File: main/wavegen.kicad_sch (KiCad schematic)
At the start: 98 parts, among them U18 CD4046, U19 CD4046, U20 CD4017, U21 CD4017, U22 TL072CP, U23 TL072CP, U24 CD4046, U25 CD4046, U26 CD4017, U27 CD4017

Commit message: Switch to Thonk jacks.
Reduces use of extended parts.
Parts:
- C52, C53, C70, C71: footprint Capacitor_SMD:C_0805_2012Metric_Pad1.18x1.45mm_HandSolder -> Capacitor_SMD:C_0603_1608Metric_Pad1.08x0.95mm_HandSolder; LCSC Part # C282698 -> C519401
- C64, C65, C74, C75: footprint Capacitor_SMD:C_0805_2012Metric_Pad1.18x1.45mm_HandSolder -> Capacitor_SMD:C_0603_1608Metric_Pad1.08x0.95mm_HandSolder; LCSC Part # C107114 -> C1658
- U20, U21, U26, U27: LCSC Part # C11349 -> C356694
- U22, U23: LCSC Part # C67473 -> C6961
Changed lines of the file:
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@@
       (effects (font (size 1.27 1.27)) hide)
     )
-    (property "LCSC Part #" "C11349" (id 5) (at 215.265 113.03 0)
+    (property "LCSC Part #" "C356694" (id 5) (at 215.265 113.03 0)
       (effects (font (size 1.27 1.27)) hide)
     )
@@
       (effects (font (size 1.27 1.27)) hide)
     )
-    (property "LCSC Part #" "C67473" (id 6) (at 125.73 37.465 0)
+    (property "LCSC Part #" "C6961" (id 6) (at 125.73 37.465 0)
       (effects (font (size 1.27 1.27)) hide)
     )
@@
       (effects (font (size 1.27 1.27)) (justify left))
     )
-    (property "Footprint" "Capacitor_SMD:C_0805_2012Metric_Pad1.18x1.45mm_HandSolder" (id 2) (at 264.16 19.05 0)
+    (property "Footprint" "Capacitor_SMD:C_0603_1608Metric_Pad1.08x0.95mm_HandSolder" (id 2) (at 264.16 19.05 0)
       (effects (font (size 1.27 1.27)) hide)
     )
@@
       (effects (font (size 1.27 1.27)) hide)
     )
-    (property "LCSC Part #" "C107114" (id 5) (at 264.16 19.05 0)
+    (property "LCSC Part #" "C1658" (id 5) (at 264.16 19.05 0)
       (effects (font (size 1.27 1.27)) hide)
     )
@@
       (effects (font (size 1.27 1.27)) hide)
     )
-    (property "LCSC Part #" "C67473" (id 6) (at 126.365 107.95 0)
+    (property "LCSC Part #" "C6961" (id 6) (at 126.365 107.95 0)
       (effects (font (size 1.27 1.27)) hide)
     )
@@
       (effects (font (size 1.27 1.27)) (justify left))
     )
-    (property "Footprint" "Capacitor_SMD:C_0805_2012Metric_Pad1.18x1.45mm_HandSolder" (id 2) (at 126.365 19.05 0)
+    (property "Footprint" "Capacitor_SMD:C_0603_1608Metric_Pad1.08x0.95mm_HandSolder" (id 2) (at 126.365 19.05 0)
       (effects (font (size 1.27 1.27)) hide)
     )
@@
       (effects (font (size 1.27 1.27)) hide)
     )
-    (property "LCSC Part #" "C107114" (id 5) (at 126.365 19.05 0)
+    (property "LCSC Part #" "C1658" (id 5) (at 126.365 19.05 0)
       (effects (font (size 1.27 1.27)) hide)
     )
@@
       (effects (font (size 1.27 1.27)) (justify left))
     )
-    (property "Footprint" "Capacitor_SMD:C_0805_2012Metric_Pad1.18x1.45mm_HandSolder" (id 2) (at 264.16 89.535 0)
+    (property "Footprint" "Capacitor_SMD:C_0603_1608Metric_Pad1.08x0.95mm_HandSolder" (id 2) (at 264.16 89.535 0)
       (effects (font (size 1.27 1.27)) hide)
     )
@@
       (effects (font (size 1.27 1.27)) hide)
     )
-    (property "LCSC Part #" "C107114" (id 5) (at 264.16 89.535 0)
+    (property "LCSC Part #" "C1658" (id 5) (at 264.16 89.535 0)
       (effects (font (size 1.27 1.27)) hide)
     )
@@
       (effects (font (size 1.27 1.27)) hide)
     )
-    (property "LCSC Part #" "C67473" (id 6) (at 262.255 37.465 0)
+    (property "LCSC Part #" "C6961" (id 6) (at 262.255 37.465 0)
       (effects (font (size 1.27 1.27)) hide)
     )
@@
       (effects (font (size 1.27 1.27)) hide)
     )
-    (property "LCSC Part #" "C11349" (id 5) (at 77.47 42.545 0)
+    (property "LCSC Part #" "C356694" (id 5) (at 77.47 42.545 0)
       (effects (font (size 1.27 1.27)) hide)
     )
@@
       (effects (font (size 1.27 1.27)) (justify left))
     )
-    (property "Footprint" "Capacitor_SMD:C_0805_2012Metric_Pad1.18x1.45mm_HandSolder" (id 2) (at 127 89.535 0)
+    (property "Footprint" "Capacitor_SMD:C_0603_1608Metric_Pad1.08x0.95mm_HandSolder" (id 2) (at 127 89.535 0)
       (effects (font (size 1.27 1.27)) hide)
     )
@@
       (effects (font (size 1.27 1.27)) hide)
     )
-    (property "LCSC Part #" "C107114" (id 5) (at 127 89.535 0)
+    (property "LCSC Part #" "C1658" (id 5) (at 127 89.535 0)
       (effects (font (size 1.27 1.27)) hide)
     )
@@
       (effects (font (size 1.27 1.27)) hide)
     )
-    (property "LCSC Part #" "C11349" (id 5) (at 77.47 113.03 0)
+    (property "LCSC Part #" "C356694" (id 5) (at 77.47 113.03 0)
       (effects (font (size 1.27 1.27)) hide)
     )
@@
       (effects (font (size 1.27 1.27)) (justify left))
     )
-    (property "Footprint" "Capacitor_SMD:C_0805_2012Metric_Pad1.18x1.45mm_HandSolder" (id 2) (at 18.415 109.22 0)
+    (property "Footprint" "Capacitor_SMD:C_0603_1608Metric_Pad1.08x0.95mm_HandSolder" (id 2) (at 18.415 109.22 0)
       (effects (font (size 1.27 1.27)) hide)
     )
@@
       (effects (font (size 1.27 1.27)) hide)
     )
-    (property "LCSC Part #" "C282698" (id 5) (at 18.415 109.22 0)
+    (property "LCSC Part #" "C519401" (id 5) (at 18.415 109.22 0)
       (effects (font (size 1.27 1.27)) hide)
     )
@@
       (effects (font (size 1.27 1.27)) (justify left))
     )
-    (property "Footprint" "Capacitor_SMD:C_0805_2012Metric_Pad1.18x1.45mm_HandSolder" (id 2) (at 156.21 38.735 0)
+    (property "Footprint" "Capacitor_SMD:C_0603_1608Metric_Pad1.08x0.95mm_HandSolder" (id 2) (at 156.21 38.735 0)
       (effects (font (size 1.27 1.27)) hide)
     )
@@
       (effects (font (size 1.27 1.27)) hide)
     )
-    (property "LCSC Part #" "C282698" (id 5) (at 156.21 38.735 0)
+    (property "LCSC Part #" "C519401" (id 5) (at 156.21 38.735 0)
       (effects (font (size 1.27 1.27)) hide)
     )
@@
       (effects (font (size 1.27 1.27)) hide)
     )
-    (property "LCSC Part #" "C67473" (id 6) (at 262.255 107.95 0)
+    (property "LCSC Part #" "C6961" (id 6) (at 262.255 107.95 0)
       (effects (font (size 1.27 1.27)) hide)
     )
@@
       (effects (font (size 1.27 1.27)) hide)
     )
-    (property "LCSC Part #" "C11349" (id 5) (at 215.265 42.545 0)
+    (property "LCSC Part #" "C356694" (id 5) (at 215.265 42.545 0)
       (effects (font (size 1.27 1.27)) hide)
     )
@@
       (effects (font (size 1.27 1.27)) hide)
     )
-    (property "LCSC Part #" "C67473" (id 4) (at 124.46 160.655 0)
+    (property "LCSC Part #" "C6961" (id 4) (at 124.46 160.655 0)
       (effects (font (size 1.27 1.27)) hide)
     )
@@
       (effects (font (size 1.27 1.27)) hide)
     )
-    (property "LCSC Part #" "C67473" (id 4) (at 135.89 160.655 0)
+    (property "LCSC Part #" "C6961" (id 4) (at 135.89 160.655 0)
       (effects (font (size 1.27 1.27)) hide)
     )
@@
       (effects (font (size 1.27 1.27)) (justify left))
     )
-    (property "Footprint" "Capacitor_SMD:C_0805_2012Metric_Pad1.18x1.45mm_HandSolder" (id 2) (at 18.415 38.735 0)
+    (property "Footprint" "Capacitor_SMD:C_0603_1608Metric_Pad1.08x0.95mm_HandSolder" (id 2) (at 18.415 38.735 0)
       (effects (font (size 1.27 1.27)) hide)
     )
@@
       (effects (font (size 1.27 1.27)) hide)
     )
-    (property "LCSC Part #" "C282698" (id 5) (at 18.415 38.735 0)
+    (property "LCSC Part #" "C519401" (id 5) (at 18.415 38.735 0)
       (effects (font (size 1.27 1.27)) hide)
     )
@@
       (effects (font (size 1.27 1.27)) (justify left))
     )
-    (property "Footprint" "Capacitor_SMD:C_0805_2012Metric_Pad1.18x1.45mm_HandSolder" (id 2) (at 156.845 109.22 0)
+    (property "Footprint" "Capacitor_SMD:C_0603_1608Metric_Pad1.08x0.95mm_HandSolder" (id 2) (at 156.845 109.22 0)
       (effects (font (size 1.27 1.27)) hide)
     )
@@
       (effects (font (size 1.27 1.27)) hide)
     )
-    (property "LCSC Part #" "C282698" (id 5) (at 156.845 109.22 0)
-      (effects (font (size 1.27 1.27)) hide)
-    )
+    (property "LCSC Part #" "C519401" (id 5) (at 156.845 109.22 0)
+      (effects (font (size 1.27 1.27)) hide)
+    )

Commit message: Version 1.0
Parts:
- added TP4, TP5, TP6, TP7: TestPoint, TestPoint:TestPoint_Loop_D2.54mm_Drill1.5mm_Beaded, symbol Connector:TestPoint
- C52, C53, C70, C71: value 300p -> 680p; LCSC Part # C519401 -> C107055
- C64, C65, C74, C75: value 30p -> 100p; LCSC Part # C1658 -> C14858
- R108, R109, R78, R79: value 332K -> 52.3K; LCSC Part # C403165 -> C23198
- RV6, RV7, RV8, RV9: footprint sputterizer:Potentiometer_Bourns_3224W_Vertical -> Potentiometer_SMD:Potentiometer_Bourns_3224W_Vertical
- U18, U19, U24, U25: Digi-Key Part (none) -> 296-32888-5-ND
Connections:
- net OSC1: now also TP4.1
- net OSC2: now also TP6.1
- net OSC3: now also TP5.1
- net OSC4: now also TP7.1
- net VC1: now reaches R52.2, R53.1, U18.9 (VCOin)
- net VC2: now reaches R82.2, R83.1, U24.9 (VCOin)
- net VC4: now reaches R84.2, R85.1, U25.9 (VCOin)
- net VC3: now reaches R54.2, R55.1, U19.9 (VCOin)
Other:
- note added: "Output: approx. -3dBm @600ohms 1.549Vp-p .547VRMS"
- note removed: "5Vpeak"

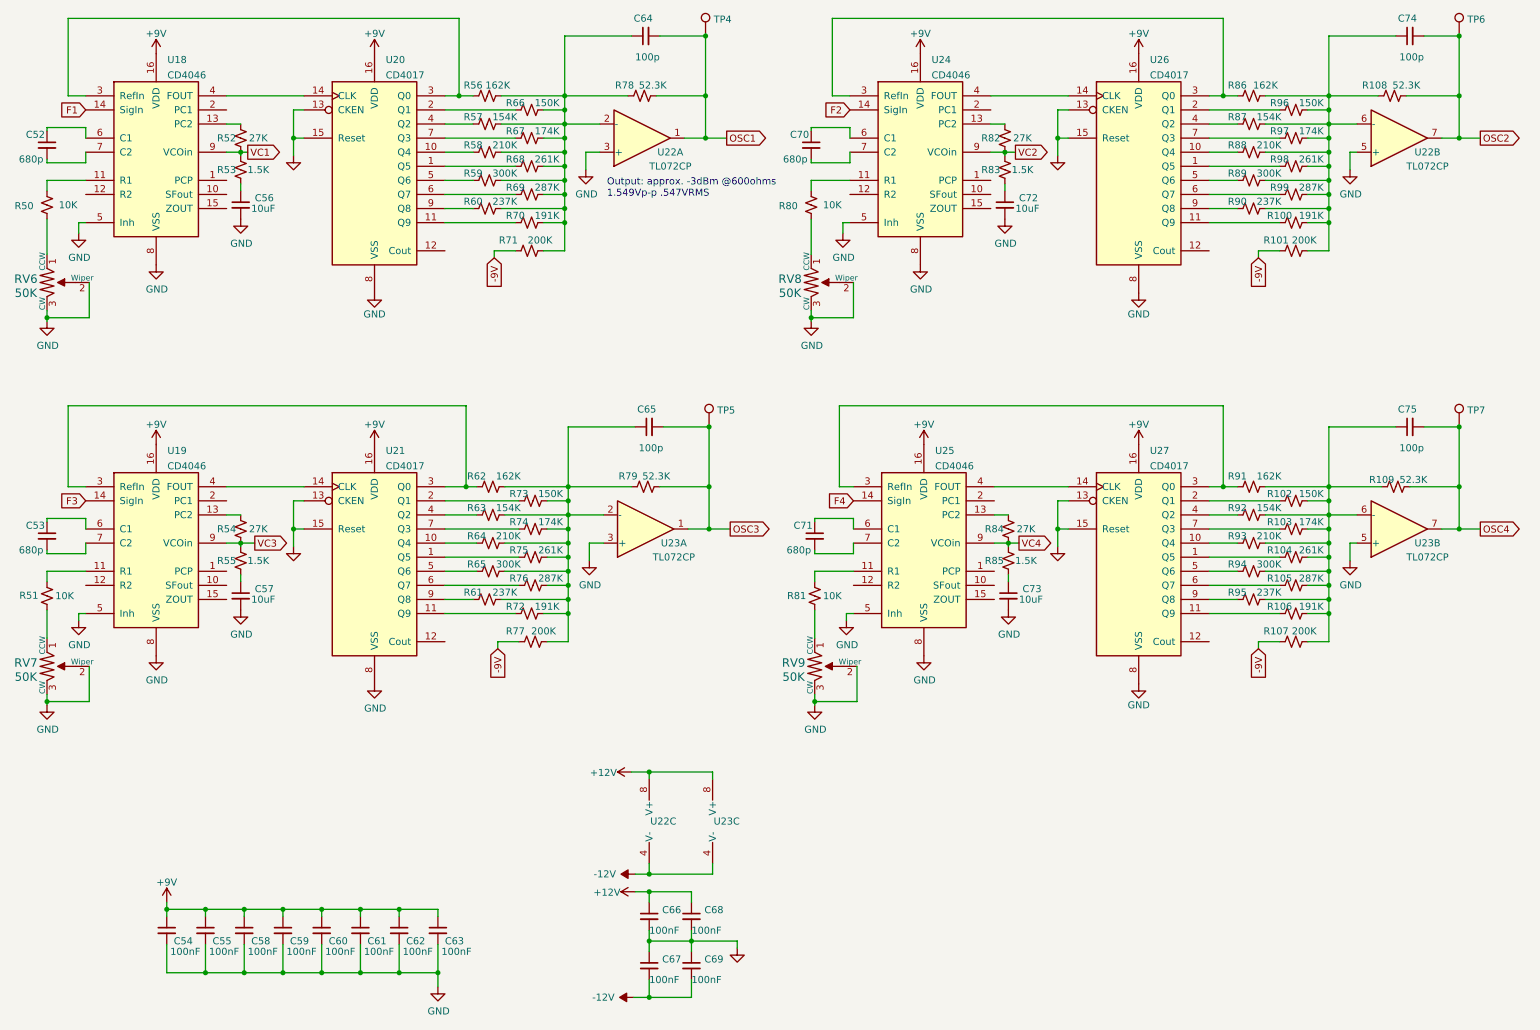
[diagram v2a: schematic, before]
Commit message: v1.0
Docs still need work.
Oscillators.sch not used. Saved just in case.
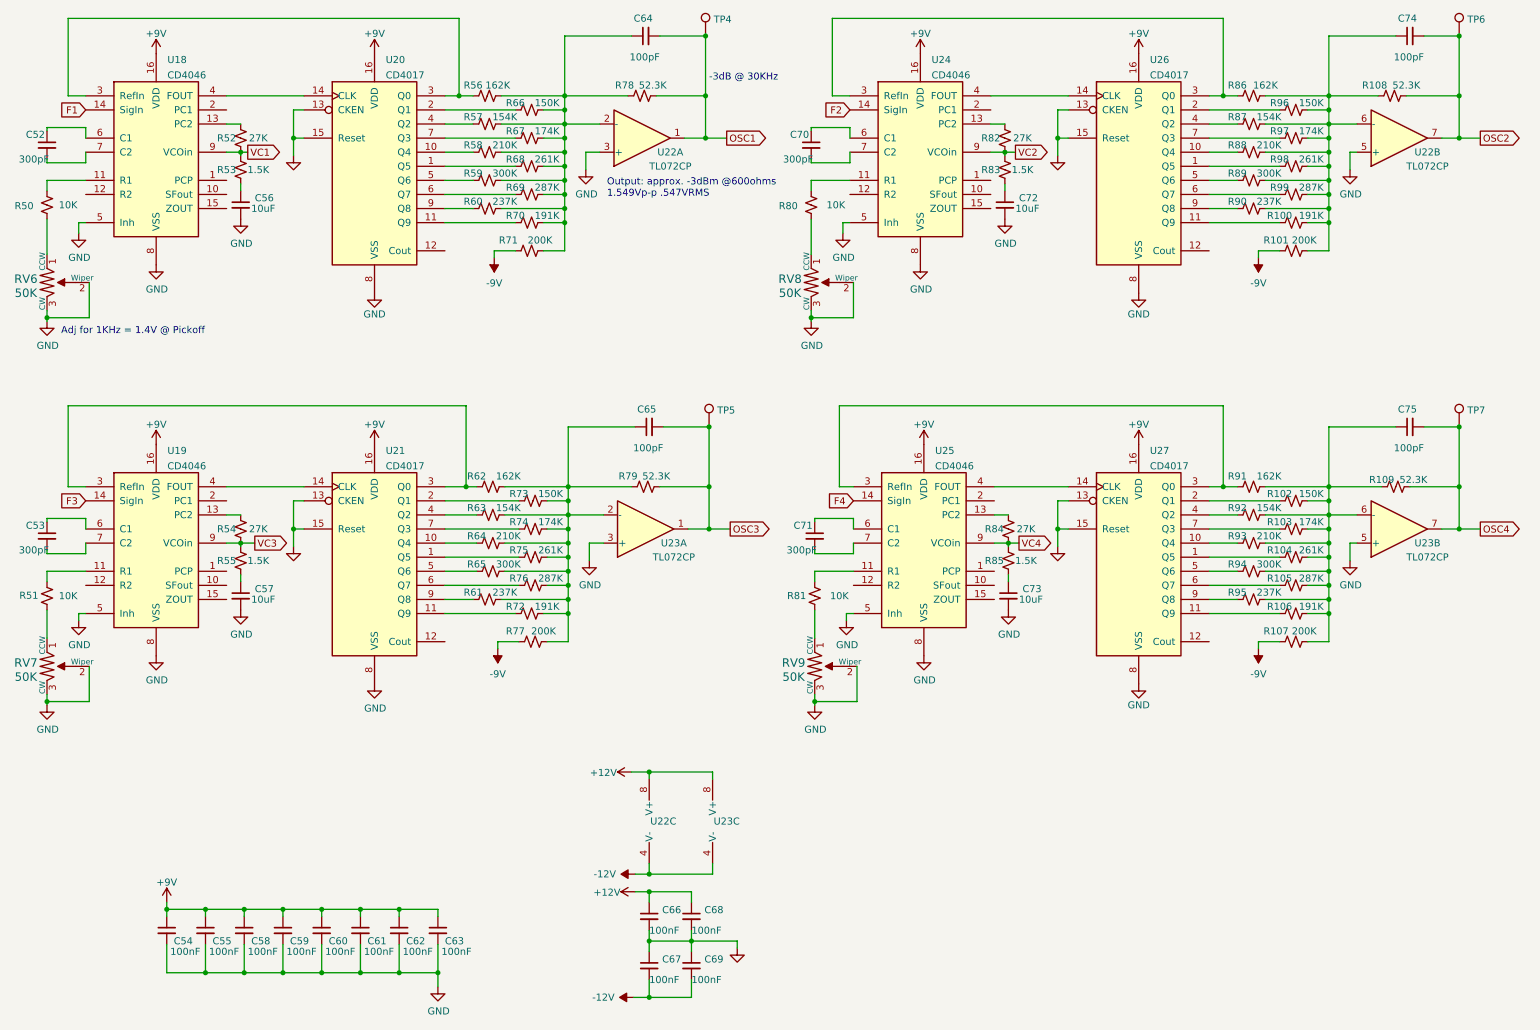
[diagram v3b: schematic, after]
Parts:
- C52, C53, C70, C71: value 680p -> 300pF; LCSC Part # C107055 -> C519401
- C64, C65, C74, C75: value 100p -> 100pF
- RV6, RV7, RV8, RV9: footprint Potentiometer_SMD:Potentiometer_Bourns_3224W_Vertical -> sputterizer:HDK_3mm; Digi-Key Part 490-2881-ND -> 118-TC33X-1-503ECT-ND; LCSC Part # C48484 -> C145161
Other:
- note added: "-3dB @ 30KHz"
- note added: "Adj for 1KHz = 1.4V @ Pickoff"

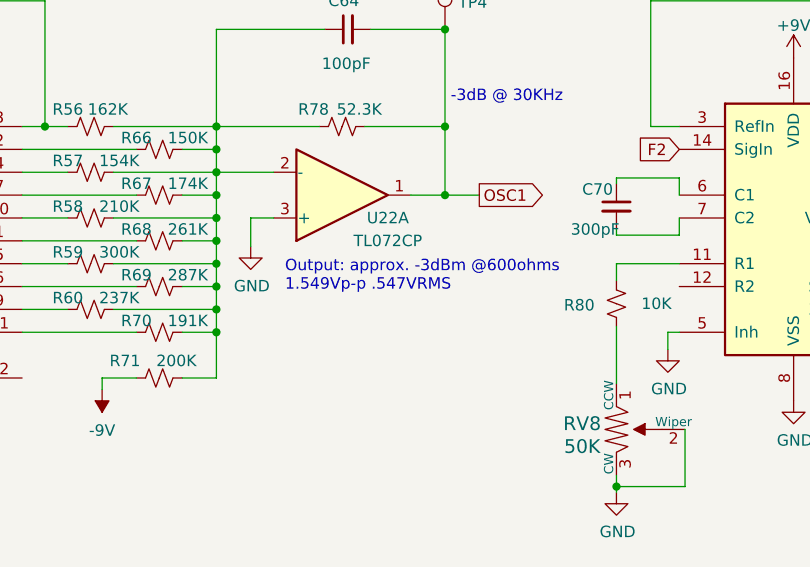
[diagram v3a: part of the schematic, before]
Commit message: Work in progress
Adds User Manual
Changes CV range to 0 - 8V
Adds spice vactrol test circuit.
Adds VCA spice study
Updates other spice and excel files.
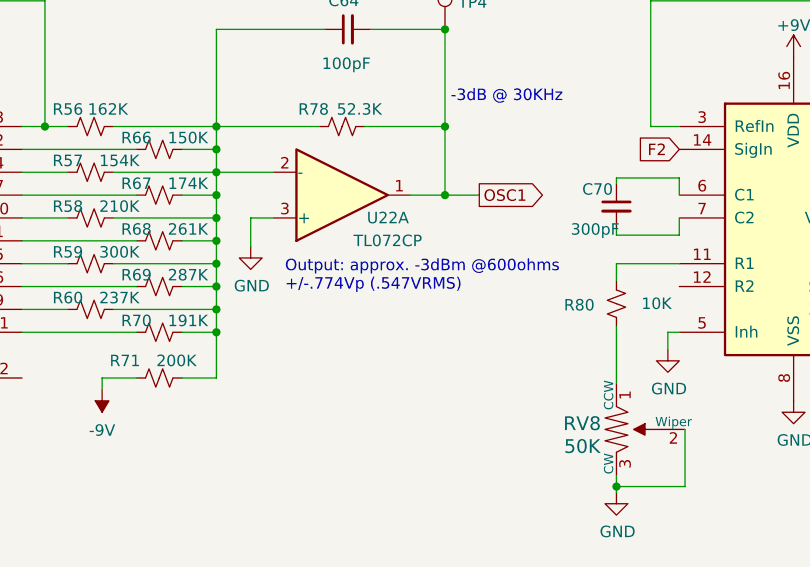
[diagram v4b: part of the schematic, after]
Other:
- note added: "Output: approx. -3dBm @600ohms +/-.774Vp (.547VRMS)"
- note removed: "Output: approx. -3dBm @600ohms 1.549Vp-p .547VRMS"
- title: (none) -> Twangilizer
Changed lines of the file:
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@@
   (paper "A4")
   (title_block
-    (rev "1.0")
+    (title "Twangilizer")
+    (rev "1.1")
   )
   (junction (at 81.915 187.96) (diameter 0) (color 0 0 0 0)
@@
     (effects (font (size 1.27 1.27)) (justify left bottom))
   )
-  (text "Output: approx. -3dBm @600ohms\n1.549Vp-p .547VRMS" (at 119.38 48.26 0)
+  (text "Output: approx. -3dBm @600ohms\n+/-.774Vp (.547VRMS)"
+    (at 119.38 48.26 0)
     (effects (font (size 1.27 1.27)) (justify left bottom))
   )
